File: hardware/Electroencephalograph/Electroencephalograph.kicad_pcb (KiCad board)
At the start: 2 copper layers, 90 x 85 mm, 304 parts, among them J1 Conn_01x08_Male, J2 Conn_01x08_Male, J3 Conn_01x04_Female, J4 Conn_01x04_Female, J5 USB_B_Micro, U1 ADS1298IPAG, U10 TPS60403, U11 GD25D10BOIGR, U2 OPA330xxD, U3 STM32F030K6Tx, U4 THI3-0511, U5 ADUM2401BRWZ, U6 FT200XD, U7 LP5912-1.8DRVT, U8 LP5912-1.8DRVT, U9 LP5912-1.8DRVT, Y1 20MHz

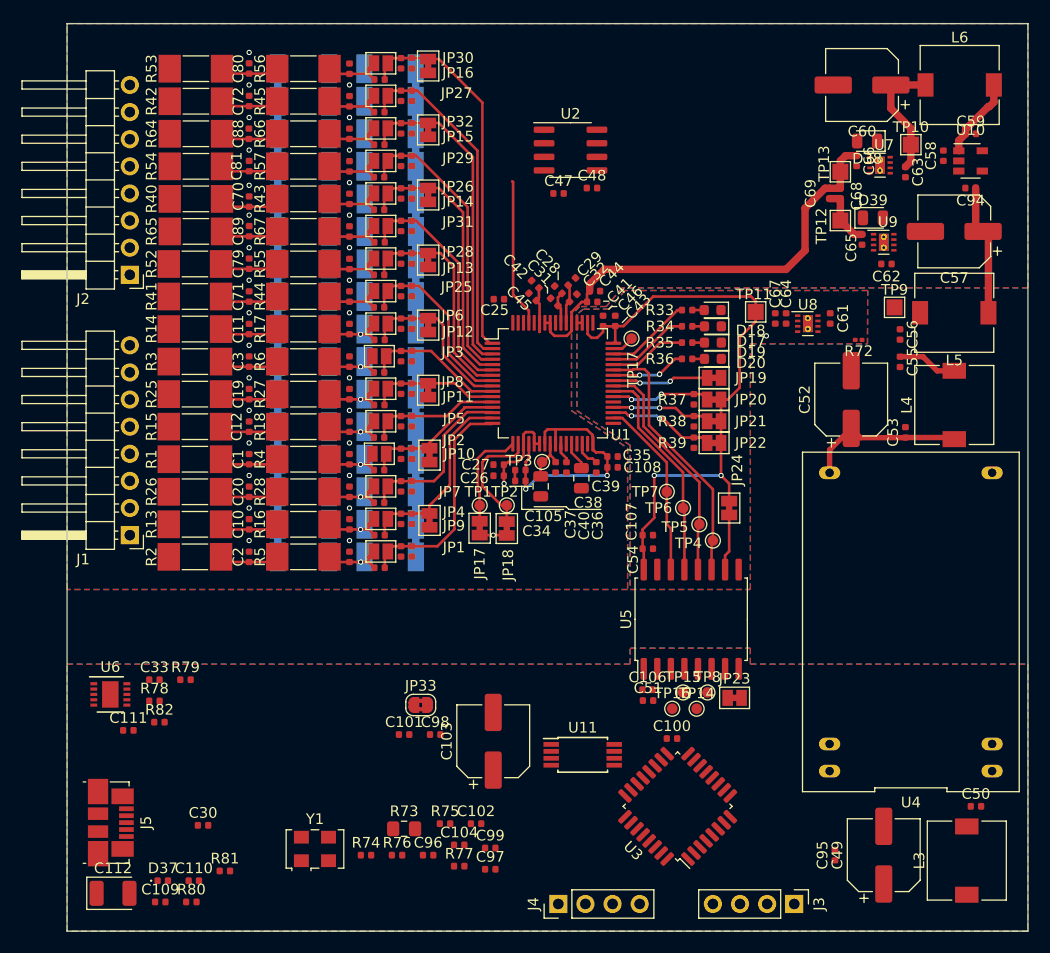
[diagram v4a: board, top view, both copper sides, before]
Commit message: reshape power supply / acquisition
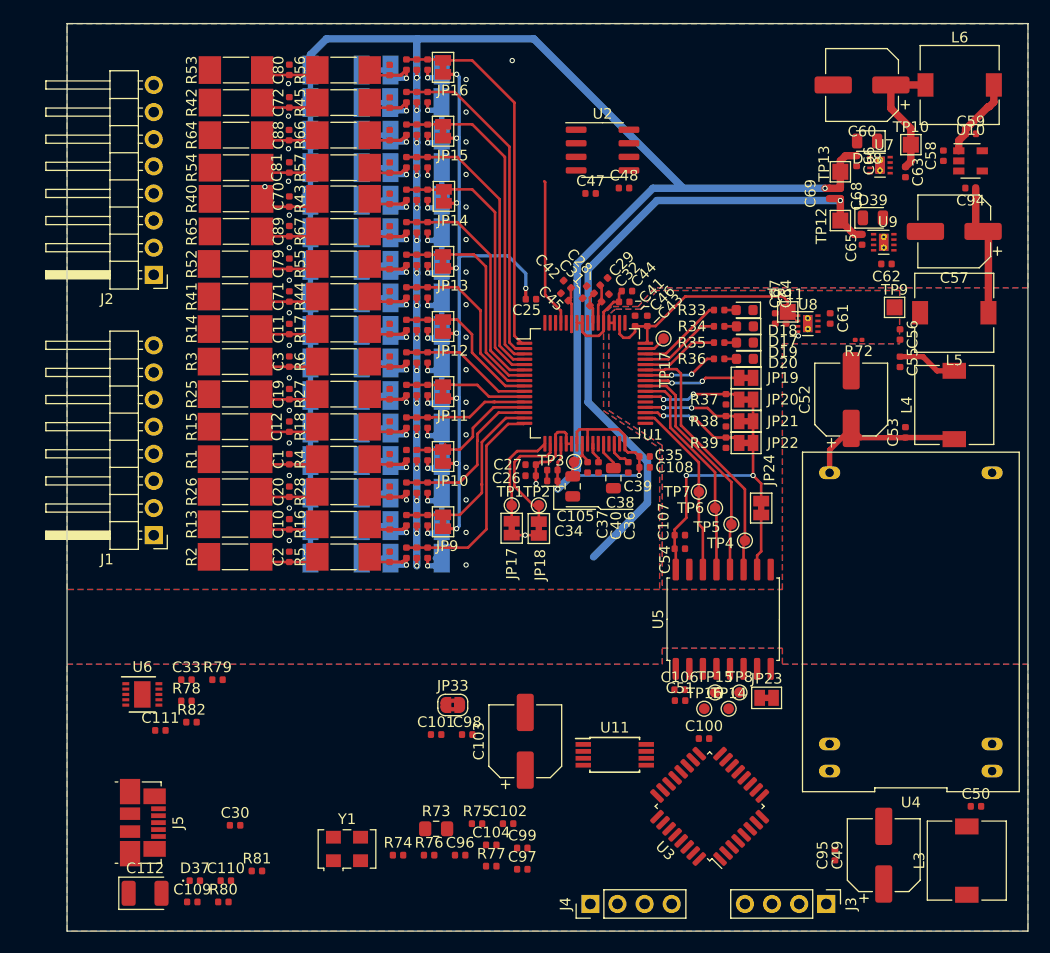
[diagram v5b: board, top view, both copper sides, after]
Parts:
- removed C16, C17, C18, C23, C24, C7, C76, C77, C78, C8, C85, C86, C87, C9, C92, C93: NC, Capacitor_SMD:C_0402_1005Metric
- removed JP1, JP2, JP25, JP26, JP27, JP28, JP29, JP3, JP30, JP31, JP32, JP4, JP5, JP6, JP7, JP8: Jumper_NO_Small, Jumper:SolderJumper-2_P1.3mm_Open_Pad1.0x1.5mm
- added R83: 0R, Resistor_SMD:R_0402_1005Metric, F.Cu at (81.8, 59.6)
- added R84: 0R, Resistor_SMD:R_0402_1005Metric, F.Cu at (81.8, 50.4)
- added R85: 0R, Resistor_SMD:R_0402_1005Metric, F.Cu at (81.8, 41.3)
- added R86: 0R, Resistor_SMD:R_0402_1005Metric, F.Cu at (81.8, 56.5)
- added R87: 0R, Resistor_SMD:R_0402_1005Metric, F.Cu at (81.8, 47.4)
- added R88: 0R, Resistor_SMD:R_0402_1005Metric, F.Cu at (81.8, 38.2)
- added R89: 0R, Resistor_SMD:R_0402_1005Metric, F.Cu at (81.8, 53.5)
- added R90: 0R, Resistor_SMD:R_0402_1005Metric, F.Cu at (81.8, 44.3)
- added R91: 0R, Resistor_SMD:R_0402_1005Metric, F.Cu at (81.8, 16.9)
- added R92: 0R, Resistor_SMD:R_0402_1005Metric, F.Cu at (81.8, 35.2)
- added R93: 0R, Resistor_SMD:R_0402_1005Metric, F.Cu at (81.8, 26.0)
- added R94: 0R, Resistor_SMD:R_0402_1005Metric, F.Cu at (81.8, 32.1)
- added R95: 0R, Resistor_SMD:R_0402_1005Metric, F.Cu at (81.8, 23.0)
- added R96: 0R, Resistor_SMD:R_0402_1005Metric, F.Cu at (81.8, 13.8)
- added R97: 0R, Resistor_SMD:R_0402_1005Metric, F.Cu at (81.8, 29.1)
- added R98: 0R, Resistor_SMD:R_0402_1005Metric, F.Cu at (81.8, 19.9)
- moved C72 3.76 mm to (70.8, 17.4)
- moved C75 3.76 mm to (80.2, 17.4)
- moved C80 3.76 mm to (70.8, 14.3)
- moved C81 3.76 mm to (70.8, 23.5)
- moved C83 3.76 mm to (80.2, 14.4)
- moved C84 3.76 mm to (80.2, 23.5)
- moved C88 3.76 mm to (70.8, 20.4)
- moved C90 3.76 mm to (80.2, 20.4)
- moved R42 3.76 mm to (65.8, 17.4)
- moved R45 3.76 mm to (75.9, 17.4)
- moved R53 3.76 mm to (65.8, 14.4)
- moved R54 3.76 mm to (65.8, 23.5)
- moved R56 3.76 mm to (75.9, 14.4)
- moved R57 3.76 mm to (75.9, 23.5)
- moved R64 3.76 mm to (65.8, 20.4)
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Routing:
- net A_VSS: track 113.3 -> 236.5 mm, vias 2 -> 20
- net A_VDD: track 67.6 -> 160.8 mm, vias 2 -> 19
- net Net-(C25-Pad1): track 0.00 -> 64.8 mm, vias 0 -> 9
- net D_VDD: track 57.3 -> 47.4 mm
- net Net-(C75-Pad1): track 5.80 -> 9.83 mm, vias 0 -> 1
- net Net-(C83-Pad1): track 5.81 -> 9.83 mm, vias 0 -> 1
- net Net-(C6-Pad1): track 5.73 -> 8.91 mm
- net Net-(C4-Pad1): track 5.73 -> 8.91 mm
- net Net-(C84-Pad1): track 5.79 -> 8.96 mm, vias 0 -> 1
- net Net-(C90-Pad1): track 5.80 -> 8.96 mm, vias 0 -> 1
- net Net-(C74-Pad1): track 5.79 -> 8.91 mm, vias 0 -> 1
- net Net-(C73-Pad1): track 5.79 -> 8.91 mm, vias 0 -> 1
- net Net-(C15-Pad1): track 5.79 -> 8.91 mm
- net Net-(C82-Pad1): track 5.79 -> 8.91 mm, vias 0 -> 1
- net Net-(C13-Pad1): track 5.81 -> 8.91 mm
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
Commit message: minor routing improvements
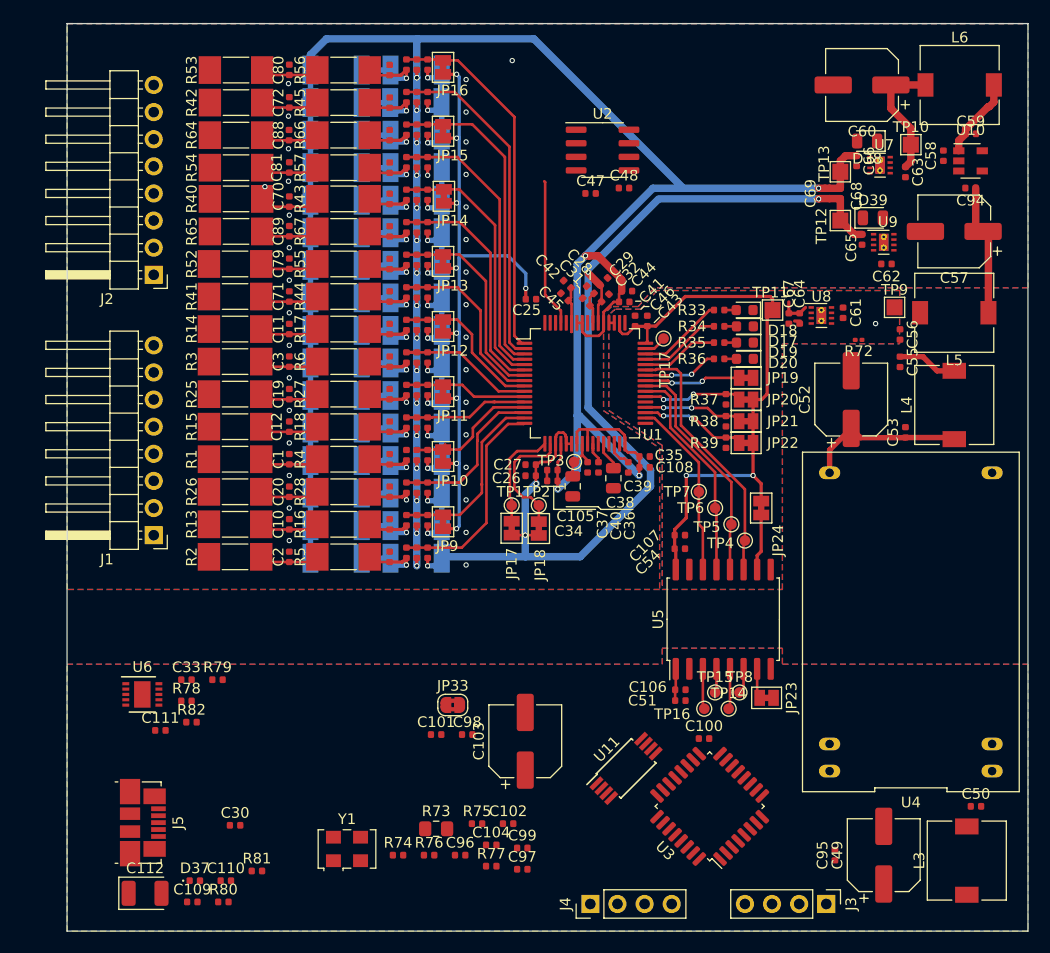
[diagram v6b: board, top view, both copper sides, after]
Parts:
- moved U11 1.66 mm to (102.4, 79.8), turned to 45 degrees
- moved U8 1.48 mm to (120.7, 37.3)
- moved TP11 1.43 mm to (116.1, 36.8)
- moved C61 1.32 mm to (122.7, 37.1)
- moved C67 1.27 mm to (117.6, 37.6)
- moved C64 1.27 mm to (118.6, 37.6)
- moved C106 0.07 mm to (107.4, 72.4)
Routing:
- net A_VDD: track 160.8 -> 181.5 mm, vias 19 -> 20
- net D_VDD: track 47.4 -> 58.4 mm
- net A_VSS: track 236.5 -> 244.2 mm, vias 20 -> 21
- net SCK: track 0.00 -> 3.78 mm
- net CS: track 0.00 -> 3.78 mm
- net DP_VDD: track 0.00 -> 2.99 mm
- net Net-(JP23-Pad1): track 0.00 -> 2.81 mm
- net MISO: track 0.00 -> 2.37 mm
- net MOSI: track 0.00 -> 2.26 mm
- net ECC_5N: track 20.3 -> 19.5 mm
- net ECC_8N: track 34.7 -> 33.9 mm
- net ECC_6N: track 25.1 -> 24.4 mm
- net D_GND: track 0.50 -> 1.04 mm

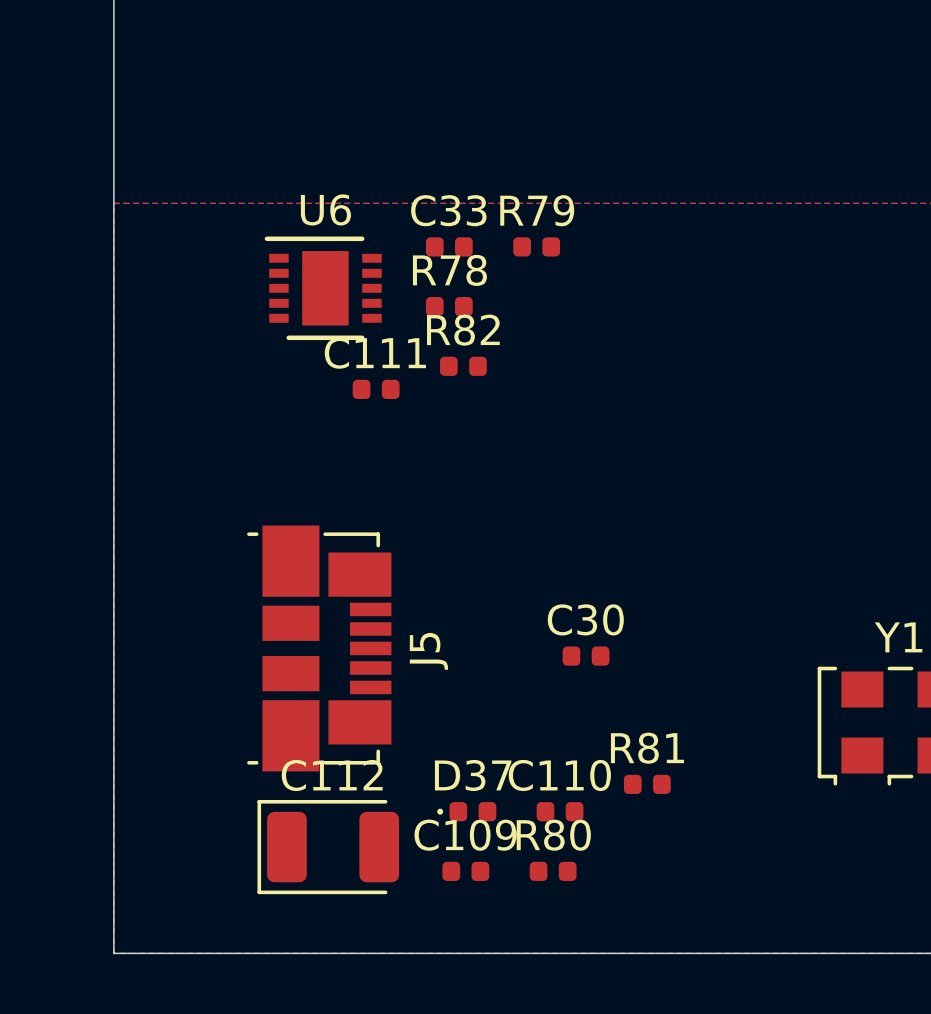
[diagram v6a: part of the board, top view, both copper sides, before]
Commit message: placement of usb interface, fix in grounds
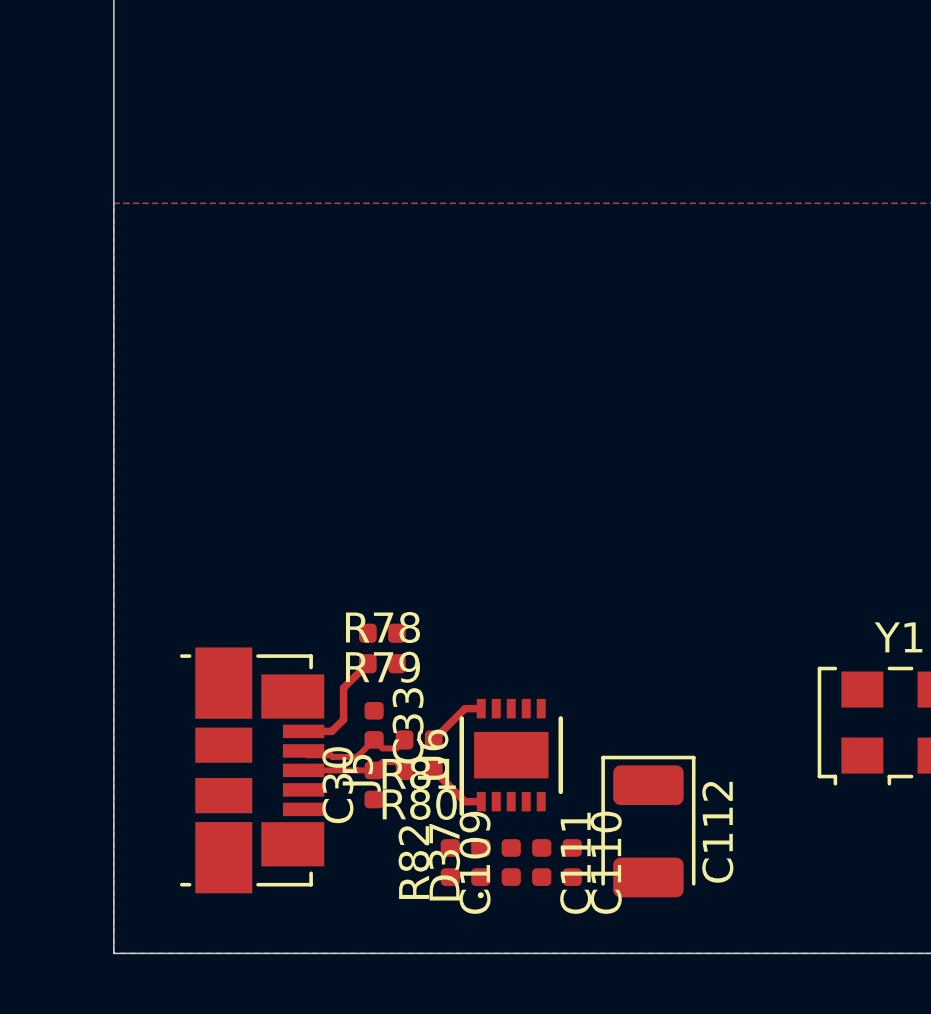
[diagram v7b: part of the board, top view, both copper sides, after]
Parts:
- moved U6 16.7 mm to (63.2, 88.4), turned to 90 degrees
- moved C111 16.7 mm to (64.3, 92.0), turned to 270 degrees
- moved R82 16.5 mm to (61.2, 92.0), turned to 90 degrees
- moved C33 16.1 mm to (58.7, 87.4), turned to 270 degrees
- moved R79 13.9 mm to (59.0, 84.3), turned to 180 degrees
- moved R78 12.1 mm to (59.0, 85.3)
- moved C112 10.5 mm to (67.8, 90.9), turned to 270 degrees
- moved C30 8.27 mm to (58.7, 89.4), turned to 90 degrees
- moved R81 7.75 mm to (60.2, 87.9), turned to 180 degrees
- moved R80 5.59 mm to (60.2, 88.9), turned to 180 degrees
- moved J5 4.64 mm to (54.9, 88.9)
- moved C110 1.74 mm to (65.3, 92.0), turned to 270 degrees
- moved D37 1.72 mm to (62.2, 92.0), turned to 90 degrees
- moved C109 1.54 mm to (63.2, 92.0), turned to 90 degrees
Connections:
- C100 pad 2: GND -> DP_GND
- C101 pad 2: GND -> DP_GND
- C102 pad 2: GND -> DP_GND
- C103 pad 2: GND -> DP_GND
- C104 pad 2: GND -> DP_GND
- C109 pad 1: GND -> DP_GND
- C110 pad 2: GND -> DP_GND
- C111 pad 2: GND -> DP_GND
- C112 pad 2: GND -> DP_GND
- C30 pad 1: GND -> DP_GND
- C33 pad 1: GND -> DP_GND
- C96 pad 1: GND -> DP_GND
- C97 pad 1: GND -> DP_GND
- C98 pad 2: GND -> DP_GND
- C99 pad 2: GND -> DP_GND
- J3 pad 2: GND -> DP_GND
- J4 pad 1: GND -> DP_GND
- J5 pad 4: GND -> DP_GND
- J5 pad 5: GND -> DP_GND
- J5 pad 6: GND -> DP_GND
- JP33 pad 1: GND -> DP_GND
- R79 pad 2: GND -> DP_GND
- R82 pad 2: GND -> DP_GND
- U3 pad 16: GND -> DP_GND
- U3 pad 32: GND -> DP_GND
- U6 pad 11: GND -> DP_GND
- U6 pad 9: GND -> DP_GND
- Y1 pad 2: GND -> DP_GND
- Y1 pad 4: GND -> DP_GND
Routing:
- net /ComputerInterface/D-: track 0.00 -> 3.92 mm
- net Net-(J5-Pad1): track 0.00 -> 3.69 mm
- net /ComputerInterface/D+: track 0.00 -> 3.60 mm
- net /ComputerInterface/DU-: track 0.00 -> 2.02 mm
- net /ComputerInterface/DU+: track 0.00 -> 2.02 mm

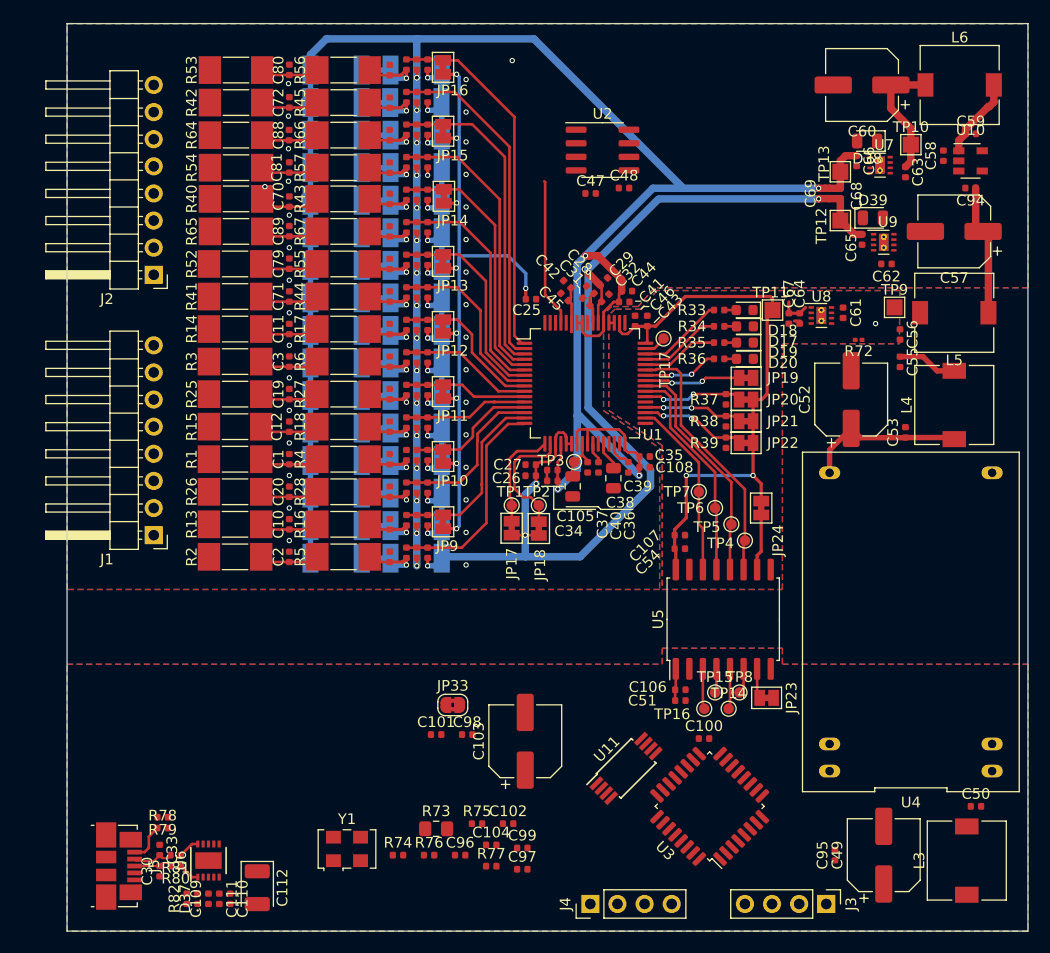
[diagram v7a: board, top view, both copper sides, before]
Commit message: fix #41, fix #18
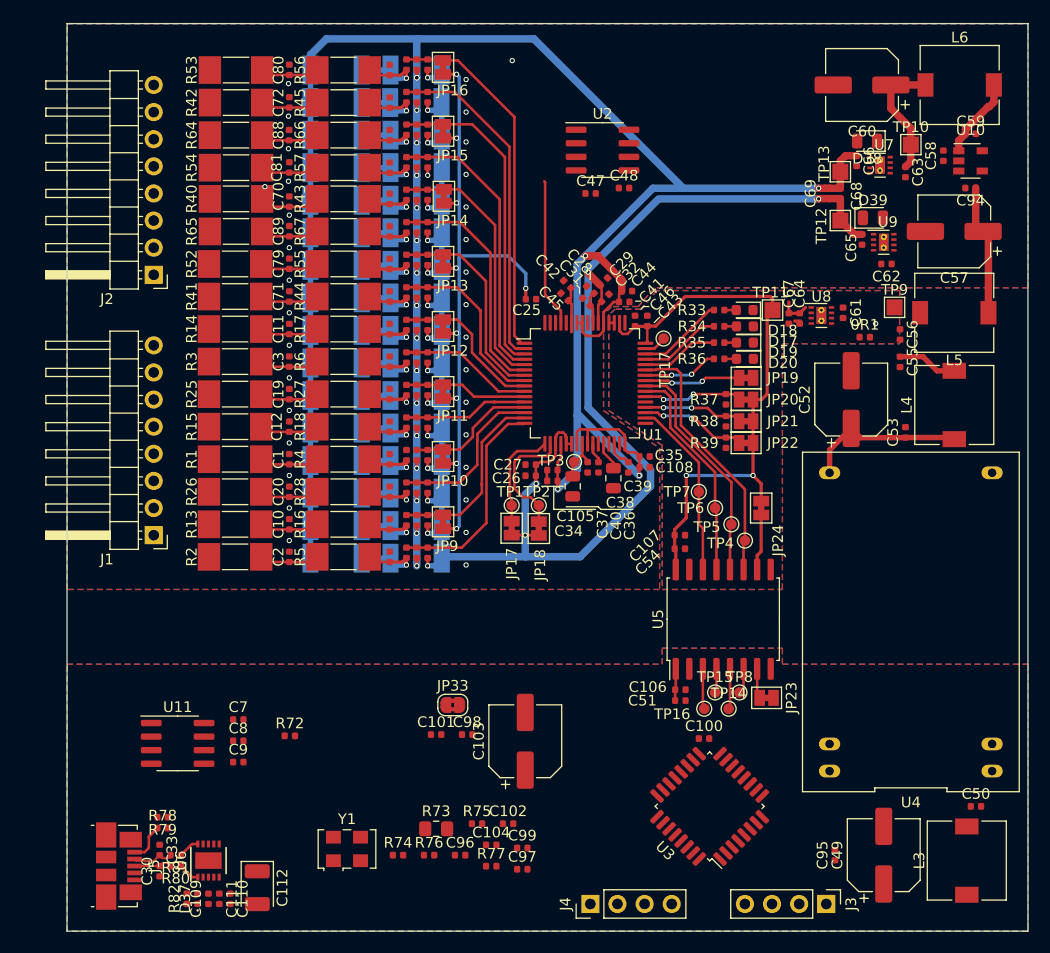
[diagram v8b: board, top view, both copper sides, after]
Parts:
- added 0R1: 10k, Resistor_SMD:R_0402_1005Metric, F.Cu at (124.7, 39.4)
- added C7: 330n, Capacitor_SMD:C_0402_1005Metric, F.Cu at (66.0, 75.2)
- added C8: 100n, Capacitor_SMD:C_0402_1005Metric, F.Cu at (66.0, 77.2)
- added C9: 100n, Capacitor_SMD:C_0402_1005Metric, F.Cu at (66.0, 79.2)
- R72: footprint Resistor_SMD:R_0201_0603Metric -> Resistor_SMD:R_0402_1005Metric
- U11: value GD25D10BOIGR -> L78L33_SO8; footprint Package_SO:TSSOP-8_4.4x3mm_P0.65mm -> Package_SO:SOIC-8_3.9x4.9mm_P1.27mm
- moved R72 64.9 mm to (70.9, 76.7), turned to 0 degrees
- moved U11 42.1 mm to (60.4, 77.4), turned to 0 degrees
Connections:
- C100 pad 1: 5V_DIGITAL -> DP_VDD
- C101 pad 1: 5V_DIGITAL -> DP_VDD
- C102 pad 1: 5V_DIGITAL -> DP_VDD
- C103 pad 1: 5V_DIGITAL -> DP_VDD
- C110 pad 1: 5V_DIGITAL -> Net-(C110-Pad1)
- C111 pad 1: 5V_DIGITAL -> Net-(C110-Pad1)
- C112 pad 1: 5V_DIGITAL -> Net-(C110-Pad1)
- C98 pad 1: 5V_DIGITAL -> DP_VDD
- C99 pad 1: 5V_DIGITAL -> DP_VDD
- J4 pad 4: 5V_DIGITAL -> DP_VDD
- R72 pad 1: A_GND -> DP_VDD
- R72 pad 2: D_GND -> Net-(C110-Pad1)
- R73 pad 1: 5V_DIGITAL -> DP_VDD
- R74 pad 1: 5V_DIGITAL -> DP_VDD
- R75 pad 1: 5V_DIGITAL -> DP_VDD
- U11 pad 1: (no net) -> DP_VDD
- U11 pad 2: (no net) -> DP_GND
- U11 pad 3: (no net) -> DP_GND
- U11 pad 6: (no net) -> DP_GND
- U11 pad 7: (no net) -> DP_GND
- U11 pad 8: (no net) -> +9V
- U3 pad 1: 5V_DIGITAL -> DP_VDD
- U3 pad 17: 5V_DIGITAL -> DP_VDD
- U3 pad 5: 5V_DIGITAL -> DP_VDD
- U6 pad 4: 5V_DIGITAL -> Net-(C110-Pad1)
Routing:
- net D_GND: vias 1 -> 0
- net A_GND: vias 32 -> 33
